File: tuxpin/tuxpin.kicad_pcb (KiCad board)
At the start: 2 copper layers, 35.1 x 46.9 mm, 23 parts, among them Q1 BC817, Q2 BC817, Q3 BC817, Q4 BC817, Q5 BC817, Q6 BC817, U1 PST-540, U2 MAX16054AZT

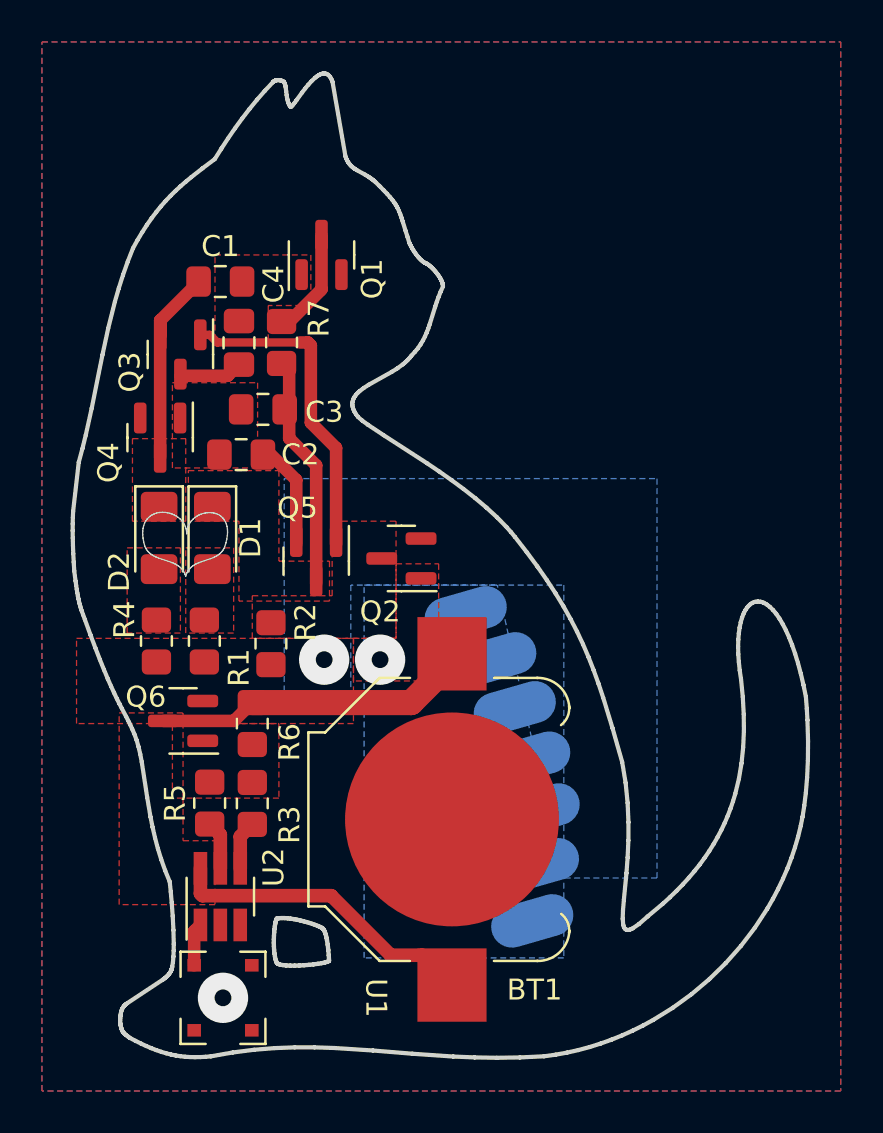
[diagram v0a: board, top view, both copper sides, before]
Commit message: changed size of the cutout in the pcb
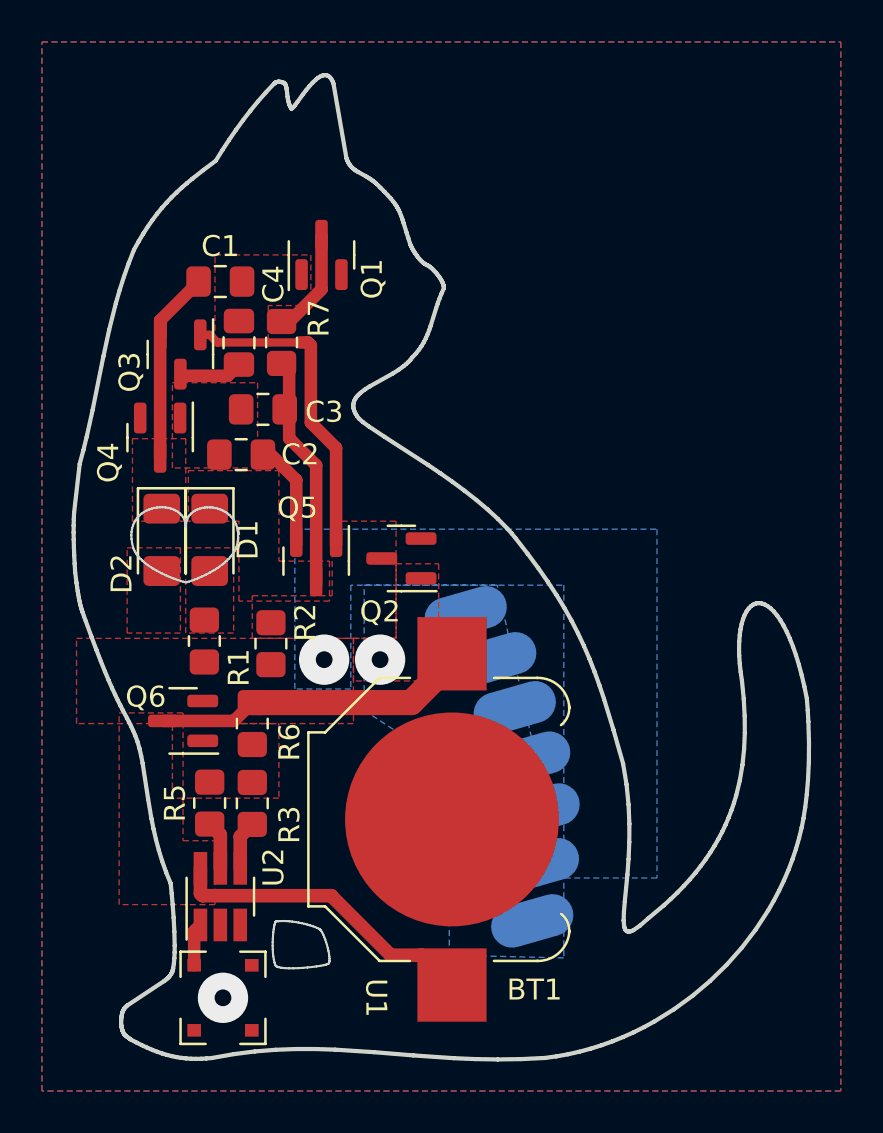
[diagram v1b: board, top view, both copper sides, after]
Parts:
- removed R4: R, Resistor_SMD:R_0805_2012Metric_Pad1.20x1.40mm_HandSolder
- moved D1 0.16 mm to (155.2, 99.4)
- moved D2 0.16 mm to (152.9, 99.4)
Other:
- outline, holes or cut-outs redrawn

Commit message: removed old gerbers, and created a updated final pcb
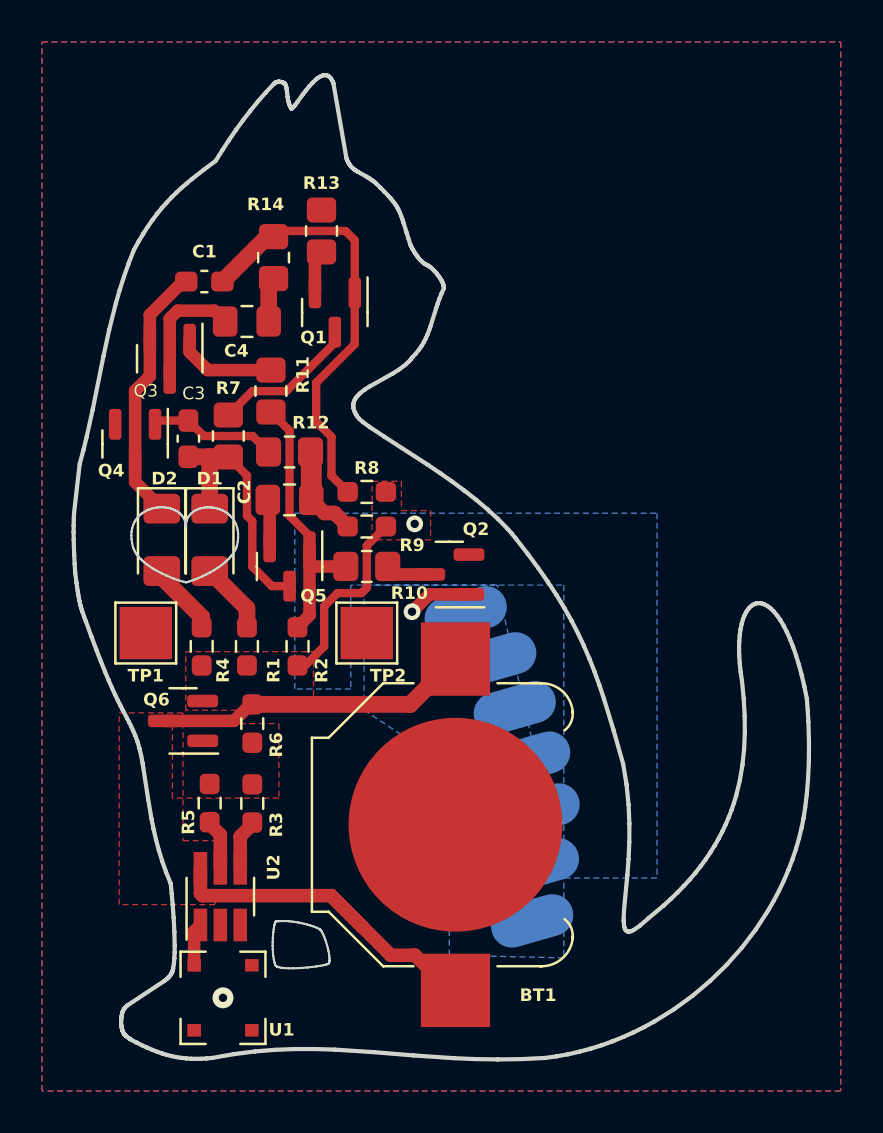
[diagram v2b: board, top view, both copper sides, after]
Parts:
- added R10: 0, Resistor_SMD:R_0805_2012Metric_Pad1.20x1.40mm_HandSolder, F.Cu at (162.7, 100.7)
- added R11: 0, Resistor_SMD:R_0805_2012Metric_Pad1.20x1.40mm_HandSolder, F.Cu at (158.1, 92.3)
- added R12: 0, Resistor_SMD:R_0805_2012Metric_Pad1.20x1.40mm_HandSolder, F.Cu at (159.0, 95.2)
- added R13: 0, Resistor_SMD:R_0805_2012Metric_Pad1.20x1.40mm_HandSolder, F.Cu at (160.5, 84.7)
- added R14: 0, Resistor_SMD:R_0805_2012Metric_Pad1.20x1.40mm_HandSolder, F.Cu at (158.2, 86.0)
- added R4: 100, Resistor_SMD:R_0603_1608Metric_Pad0.98x0.95mm_HandSolder, F.Cu at (154.8, 104.5)
- added R8: 47k, Resistor_SMD:R_0603_1608Metric_Pad0.98x0.95mm_HandSolder, F.Cu at (162.7, 97.2)
- added R9: 47k, Resistor_SMD:R_0603_1608Metric_Pad0.98x0.95mm_HandSolder, F.Cu at (162.7, 98.8)
- added TP1: TestPoint, TestPoint:TestPoint_Pad_2.5x2.5mm, F.Cu at (152.1, 103.9)
- added TP2: TestPoint, TestPoint:TestPoint_Pad_2.5x2.5mm, F.Cu at (162.7, 103.9)
- C1, C3: value C -> 10u; footprint Capacitor_SMD:C_0805_2012Metric_Pad1.18x1.45mm_HandSolder -> Capacitor_SMD:C_0603_1608Metric_Pad1.08x0.95mm_HandSolder
- C2, C4: value C -> 22u
- R1, R2: value R -> 100; footprint Resistor_SMD:R_0805_2012Metric_Pad1.20x1.40mm_HandSolder -> Resistor_SMD:R_0603_1608Metric_Pad0.98x0.95mm_HandSolder
- R3, R5, R6: footprint Resistor_SMD:R_0805_2012Metric_Pad1.20x1.40mm_HandSolder -> Resistor_SMD:R_0603_1608Metric_Pad0.98x0.95mm_HandSolder
- moved R7 5.13 mm to (156.1, 94.5)
- moved C3 3.82 mm to (154.2, 94.6), turned to -90 degrees
- moved C2 3.16 mm to (159.0, 97.5), turned to 180 degrees
- moved Q1 2.82 mm to (161.2, 88.6), turned to -90 degrees
- moved Q2 2.41 mm to (166.6, 101.1)
- moved R1 2.05 mm to (157.0, 104.5)
- moved Q5 1.30 mm to (159.0, 100.7)
- moved R2 1.28 mm to (159.4, 104.5)
- moved Q4 1.23 mm to (151.6, 94.9)
- moved C4 1.09 mm to (157.0, 89.0), turned to 180 degrees
- moved C1 0.76 mm to (154.9, 87.1)
- moved Q3 0.55 mm to (153.3, 90.8)
- moved BT1 0.30 mm to (166.9, 113.0)
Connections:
- C2 pad 1: Net-(Q4-B) -> Net-(C2-Pad1)
- C4 pad 1: Net-(Q1-B) -> Net-(C4-Pad1)
- Q1 pad 2: GND -> Net-(Q1-E)
- Q3 pad 1: Net-(Q2-C) -> Net-(Q3-B)
- Q5 pad 1: Net-(Q2-C) -> Net-(Q5-B)
- R2 pad 2: Net-(Q2-C) -> Net-(Q5-B)
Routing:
- net Net-(Q1-B): track 0.00 -> 20.9 mm
- net Net-(Q2-C): track 15.5 -> 2.16 mm
- net Net-(Q5-B): track 0.00 -> 13.0 mm
- net VCC: track 0.00 -> 9.25 mm
- net Net-(Q4-B): track 0.00 -> 6.11 mm
- net Net-(Q3-B): track 0.00 -> 4.85 mm
- net Net-(C2-Pad1): track 0.00 -> 4.57 mm
- net +3V0: track 30.5 -> 34.4 mm
- net Net-(D2-A): track 0.00 -> 3.47 mm
- net Net-(D1-A): track 0.00 -> 3.42 mm
- net Net-(Q1-C): track 10.3 -> 7.01 mm
- net Net-(Q2-B): track 0.00 -> 3.06 mm
- net Net-(Q3-C): track 3.02 -> 5.87 mm
- net Net-(D2-K): track 9.92 -> 12.5 mm
- net Net-(C4-Pad1): track 0.00 -> 2.14 mm
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- removed copper zone on F.Cu, net Net-(D1-A)
- removed copper zone on F.Cu, net Net-(D1-K)
- removed copper zone on F.Cu, net Net-(D2-A)
- removed copper zone on F.Cu, net Net-(D2-K)
- removed copper zone on F.Cu, net Net-(Q1-B)
- removed copper zone on F.Cu, net Net-(Q2-B)
- removed copper zone on F.Cu, net Net-(Q2-C)
- removed copper zone on F.Cu, net Net-(Q4-B)
